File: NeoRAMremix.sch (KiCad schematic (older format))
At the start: 27 parts, among them P1 C64-Exp-Port, Q1 2N3904, SW1 Reset, U1 HM628512BFP-5, U2 HM628512BFP-5, U3 HM628512BFP-5, U4 HM628512BFP-5

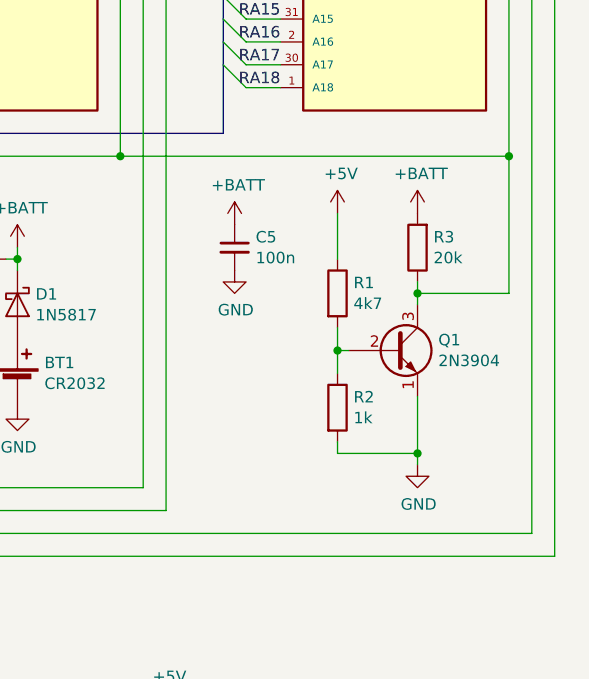
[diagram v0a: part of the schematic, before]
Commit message: Added JP1 to disable battery circuit for /CS.
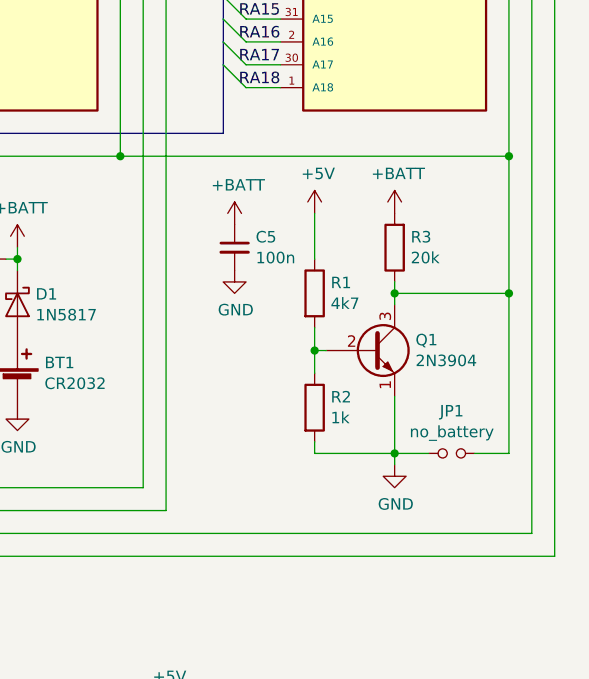
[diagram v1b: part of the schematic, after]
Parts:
- added JP1: no_battery, Pin_Headers:Pin_Header_Straight_2x01_Pitch2.54mm, symbol device:Jumper_NO_Small
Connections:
- net GND: now also JP1.1
- net at Q1.3 (C), R3.1, U1.22 (~CS)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: now also JP1.2
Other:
- moved on the sheet: Q1, R1, R2, R3
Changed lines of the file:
@@
 L device:R R3
 U 1 1 5C4878F2
-P 10400 3800
-F 0 "R3" H 10330 3754 50  0000 R CNN
-F 1 "20k" H 10330 3845 50  0000 R CNN
-F 2 "Resistors_THT:R_Axial_DIN0207_L6.3mm_D2.5mm_P2.54mm_Vertical" V 10330 3800 50  0001 C CNN
-F 3 "~" H 10400 3800 50  0001 C CNN
-	1    10400 3800
+P 10300 3800
+F 0 "R3" H 10230 3754 50  0000 R CNN
+F 1 "20k" H 10230 3845 50  0000 R CNN
+F 2 "Resistors_THT:R_Axial_DIN0207_L6.3mm_D2.5mm_P2.54mm_Vertical" V 10230 3800 50  0001 C CNN
+F 3 "~" H 10300 3800 50  0001 C CNN
+	1    10300 3800
 	-1   0    0    1
 $EndComp
@@
 L Transistor:2N3904 Q1
 U 1 1 5C494A1C
-P 10300 4250
-F 0 "Q1" H 10491 4296 50  0000 L CNN
-F 1 "2N3904" H 10491 4205 50  0000 L CNN
-F 2 "TO_SOT_Packages_THT:TO-92_Molded_Narrow" H 10500 4175 50  0001 L CIN
-F 3 "https://www.fairchildsemi.com/datasheets/2N/2N3904.pdf" H 10300 4250 50  0001 L CNN
-	1    10300 4250
+P 10200 4250
+F 0 "Q1" H 10391 4296 50  0000 L CNN
+F 1 "2N3904" H 10391 4205 50  0000 L CNN
+F 2 "TO_SOT_Packages_THT:TO-92_Molded_Narrow" H 10400 4175 50  0001 L CIN
+F 3 "https://www.fairchildsemi.com/datasheets/2N/2N3904.pdf" H 10200 4250 50  0001 L CNN
+	1    10200 4250
 	1    0    0    -1
 $EndComp
@@
 L device:R R1
 U 1 1 5C69B5F1
-P 10050 4000
-F 0 "R1" H 10120 4046 50  0000 L CNN
-F 1 "4k7" H 10120 3955 50  0000 L CNN
-F 2 "Resistors_THT:R_Axial_DIN0207_L6.3mm_D2.5mm_P2.54mm_Vertical" V 9980 4000 50  0001 C CNN
-F 3 "~" H 10050 4000 50  0001 C CNN
-	1    10050 4000
+P 9950 4000
+F 0 "R1" H 10020 4046 50  0000 L CNN
+F 1 "4k7" H 10020 3955 50  0000 L CNN
+F 2 "Resistors_THT:R_Axial_DIN0207_L6.3mm_D2.5mm_P2.54mm_Vertical" V 9880 4000 50  0001 C CNN
+F 3 "~" H 9950 4000 50  0001 C CNN
+	1    9950 4000
 	1    0    0    -1
 $EndComp
@@
 L device:R R2
 U 1 1 5C69B625
-P 10050 4500
-F 0 "R2" H 10120 4546 50  0000 L CNN
-F 1 "1k" H 10120 4455 50  0000 L CNN
-F 2 "Resistors_THT:R_Axial_DIN0207_L6.3mm_D2.5mm_P2.54mm_Vertical" V 9980 4500 50  0001 C CNN
-F 3 "~" H 10050 4500 50  0001 C CNN
-	1    10050 4500
-	1    0    0    -1
-$EndComp
-Wire Wire Line
-	10050 4350 10050 4250
-Wire Wire Line
-	10050 4250 10100 4250
-Wire Wire Line
-	10050 4650 10050 4700
-Wire Wire Line
-	10050 4700 10400 4700
-Wire Wire Line
-	10400 4700 10400 4450
+P 9950 4500
+F 0 "R2" H 10020 4546 50  0000 L CNN
+F 1 "1k" H 10020 4455 50  0000 L CNN
+F 2 "Resistors_THT:R_Axial_DIN0207_L6.3mm_D2.5mm_P2.54mm_Vertical" V 9880 4500 50  0001 C CNN
+F 3 "~" H 9950 4500 50  0001 C CNN
+	1    9950 4500
+	1    0    0    -1
+$EndComp
+Wire Wire Line
+	9950 4350 9950 4250
+Wire Wire Line
+	9950 4250 10000 4250
+Wire Wire Line
+	9950 4650 9950 4700
+Wire Wire Line
+	9950 4700 10300 4700
+Wire Wire Line
+	10300 4700 10300 4450
 $Comp
 L power:GND #PWR0116
 U 1 1 5C6F0ED2
-P 10400 4750
-F 0 "#PWR0116" H 10400 4500 50  0001 C CNN
-F 1 "GND" H 10405 4577 50  0000 C CNN
-F 2 "" H 10400 4750 50  0001 C CNN
-F 3 "" H 10400 4750 50  0001 C CNN
-	1    10400 4750
-	1    0    0    -1
-$EndComp
-Wire Wire Line
-	10400 4750 10400 4700
-Connection ~ 10400 4700
-Wire Wire Line
-	10050 4150 10050 4250
-Connection ~ 10050 4250
+P 10300 4750
+F 0 "#PWR0116" H 10300 4500 50  0001 C CNN
+F 1 "GND" H 10305 4577 50  0000 C CNN
+F 2 "" H 10300 4750 50  0001 C CNN
+F 3 "" H 10300 4750 50  0001 C CNN
+	1    10300 4750
+	1    0    0    -1
+$EndComp
+Wire Wire Line
+	10300 4750 10300 4700
+Connection ~ 10300 4700
+Wire Wire Line
+	9950 4150 9950 4250
+Connection ~ 9950 4250
 $Comp
 L power:+5V #PWR0117
 U 1 1 5C7731EA
-P 10050 3650
-F 0 "#PWR0117" H 10050 3500 50  0001 C CNN
-F 1 "+5V" H 10065 3823 50  0000 C CNN
-F 2 "" H 10050 3650 50  0001 C CNN
-F 3 "" H 10050 3650 50  0001 C CNN
-	1    10050 3650
+P 9950 3650
+F 0 "#PWR0117" H 9950 3500 50  0001 C CNN
+F 1 "+5V" H 9965 3823 50  0000 C CNN
+F 2 "" H 9950 3650 50  0001 C CNN
+F 3 "" H 9950 3650 50  0001 C CNN
+	1    9950 3650
 	1    0    0    -1
 $EndComp
@@
 	9100 3400 10800 3400
 Wire Wire Line
-	10050 3650 10050 3850
-Wire Wire Line
-	10400 3950 10400 4000
-Wire Wire Line
-	10400 4000 10800 4000
+	9950 3650 9950 3850
+Wire Wire Line
+	10300 3950 10300 4000
 Wire Wire Line
 	10800 4000 10800 3400
-Connection ~ 10400 4000
-Wire Wire Line
-	10400 4000 10400 4050
+Connection ~ 10300 4000
+Wire Wire Line
+	10300 4000 10300 4050
 Connection ~ 10800 3400
 $Comp
@@
 L power:+BATT #PWR0123
 U 1 1 5C8631B0
-P 10400 3650
-F 0 "#PWR0123" H 10400 3500 50  0001 C CNN
-F 1 "+BATT" H 10415 3823 50  0000 C CNN
-F 2 "" H 10400 3650 50  0001 C CNN
-F 3 "" H 10400 3650 50  0001 C CNN
-	1    10400 3650
+P 10300 3650
+F 0 "#PWR0123" H 10300 3500 50  0001 C CNN
+F 1 "+BATT" H 10315 3823 50  0000 C CNN
+F 2 "" H 10300 3650 50  0001 C CNN
+F 3 "" H 10300 3650 50  0001 C CNN
+	1    10300 3650
 	1    0    0    -1
 $EndComp
@@
 	4200 6250 4400 6250
 Connection ~ 4200 6750
+Wire Wire Line
+	10300 4000 10800 4000
+$Comp
+L device:Jumper_NO_Small JP1
+U 1 1 5CD1924D
+P 10550 4700
+F 0 "JP1" H 10550 4885 50  0000 C CNN
+F 1 "no_battery" H 10550 4794 50  0000 C CNN
+F 2 "Pin_Headers:Pin_Header_Straight_2x01_Pitch2.54mm" H 10550 4700 50  0001 C CNN
+F 3 "~" H 10550 4700 50  0001 C CNN
+	1    10550 4700
+	1    0    0    -1
+$EndComp
+Wire Wire Line
+	10800 4000 10800 4700
+Wire Wire Line
+	10800 4700 10650 4700
+Connection ~ 10800 4000
+Wire Wire Line
+	10450 4700 10300 4700
 Wire Bus Line
 	6150 2000 6150 3300

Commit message: Improved solder jumper footprint.
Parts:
- SJ1, SJ2, SJ3, SJ4: footprint Jumper:SolderJumper-3_P1.3mm_Bridged12_RoundedPad1.0x1.5mm -> NeoRAMremix:SolderJumper-3_P1.3mm_Bridged12
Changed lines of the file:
@@
 F 0 "SJ2" H 1000 3664 50  0000 C CNN
 F 1 "SolderJumper_3_Bridged12" H 1000 3664 50  0001 C CNN
-F 2 "Jumper:SolderJumper-3_P1.3mm_Bridged12_RoundedPad1.0x1.5mm" H 1000 3550 50  0001 C CNN
+F 2 "NeoRAMremix:SolderJumper-3_P1.3mm_Bridged12" H 1000 3550 50  0001 C CNN
 F 3 "~" H 1000 3550 50  0001 C CNN
 	1    1000 3550
@@
 F 0 "SJ1" H 1550 3664 50  0000 C CNN
 F 1 "SolderJumper_3_Bridged12" H 1550 3664 50  0001 C CNN
-F 2 "Jumper:SolderJumper-3_P1.3mm_Bridged12_RoundedPad1.0x1.5mm" H 1550 3550 50  0001 C CNN
+F 2 "NeoRAMremix:SolderJumper-3_P1.3mm_Bridged12" H 1550 3550 50  0001 C CNN
 F 3 "~" H 1550 3550 50  0001 C CNN
 	1    1550 3550
@@
 F 0 "SJ3" V 4400 6118 50  0000 L CNN
 F 1 "SolderJumper_3_Bridged12" H 4400 6164 50  0001 C CNN
-F 2 "Jumper:SolderJumper-3_P1.3mm_Bridged12_RoundedPad1.0x1.5mm" H 4400 6050 50  0001 C CNN
+F 2 "NeoRAMremix:SolderJumper-3_P1.3mm_Bridged12" H 4400 6050 50  0001 C CNN
 F 3 "~" H 4400 6050 50  0001 C CNN
 	1    4400 6050
@@
 F 0 "SJ4" V 4400 6618 50  0000 L CNN
 F 1 "SolderJumper_3_Bridged12" H 4400 6664 50  0001 C CNN
-F 2 "Jumper:SolderJumper-3_P1.3mm_Bridged12_RoundedPad1.0x1.5mm" H 4400 6550 50  0001 C CNN
+F 2 "NeoRAMremix:SolderJumper-3_P1.3mm_Bridged12" H 4400 6550 50  0001 C CNN
 F 3 "~" H 4400 6550 50  0001 C CNN
 	1    4400 6550

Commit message: Replaced JP1 with solder jumber SJ5.
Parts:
- SJ5: renamed from JP1; footprint Pin_Headers:Pin_Header_Straight_2x01_Pitch2.54mm -> Jumper:SolderJumper-2_P1.3mm_Open_RoundedPad1.0x1.5mm
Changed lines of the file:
@@
 	10300 4000 10800 4000
 $Comp
-L device:Jumper_NO_Small JP1
+L device:Jumper_NO_Small SJ5
 U 1 1 5CD1924D
 P 10550 4700
-F 0 "JP1" H 10550 4885 50  0000 C CNN
+F 0 "SJ5" H 10550 4885 50  0000 C CNN
 F 1 "no_battery" H 10550 4794 50  0000 C CNN
-F 2 "Pin_Headers:Pin_Header_Straight_2x01_Pitch2.54mm" H 10550 4700 50  0001 C CNN
+F 2 "Jumper:SolderJumper-2_P1.3mm_Open_RoundedPad1.0x1.5mm" H 10550 4700 50  0001 C CNN
 F 3 "~" H 10550 4700 50  0001 C CNN
 	1    10550 4700
